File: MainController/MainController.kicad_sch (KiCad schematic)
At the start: 0 parts

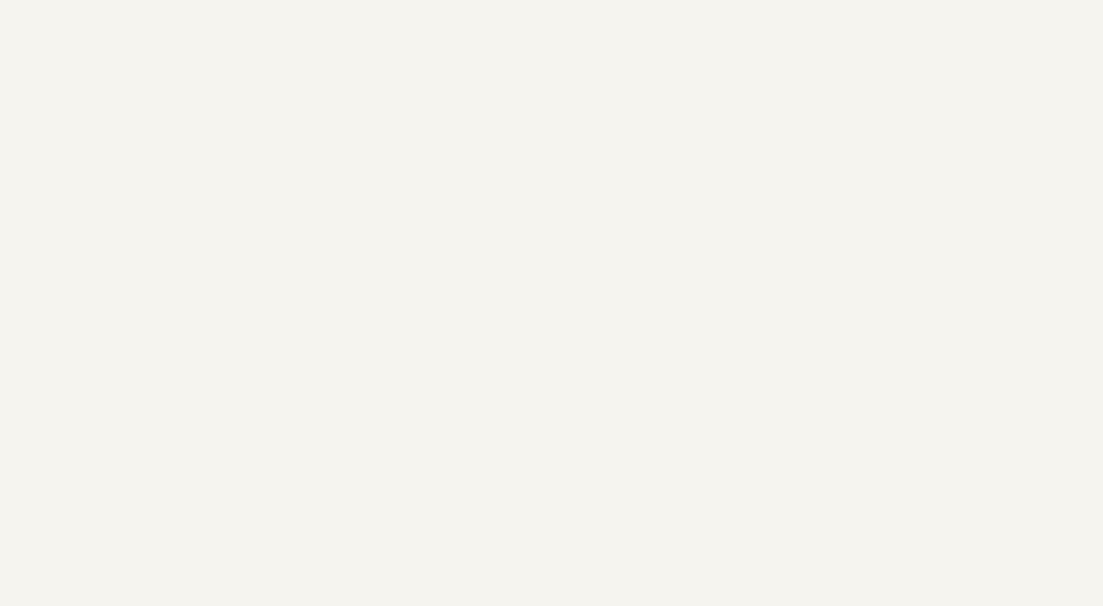
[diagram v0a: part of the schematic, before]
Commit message: WIP - Starting Voltage Measurement
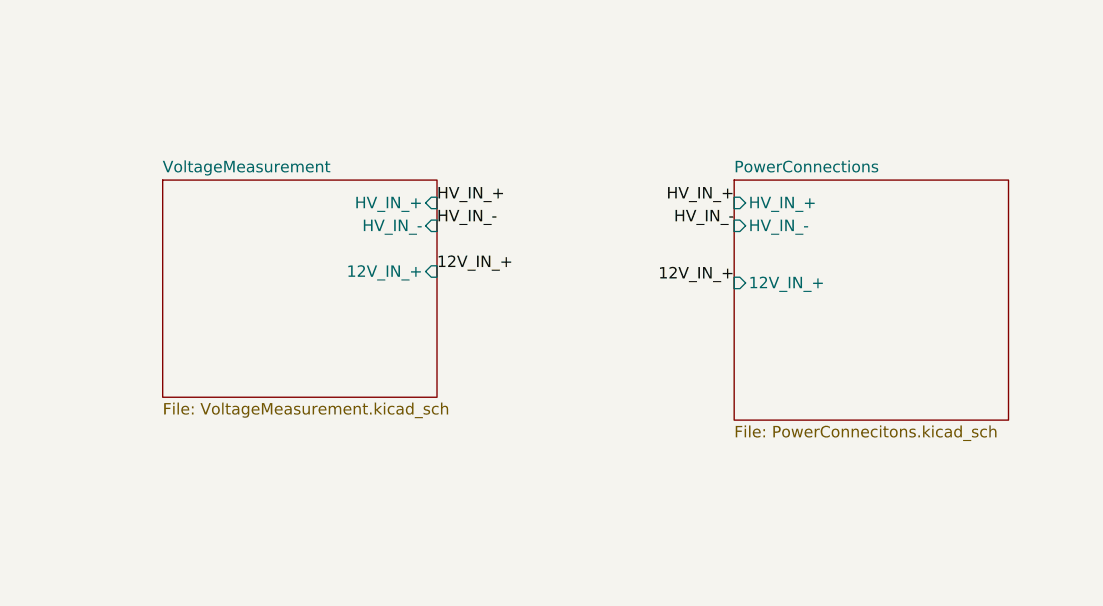
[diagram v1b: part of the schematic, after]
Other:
- added sheet PowerConnections (PowerConnecitons.kicad_sch)
- added sheet VoltageMeasurement (VoltageMeasurement.kicad_sch)
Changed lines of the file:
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@@
 	(generator_version "8.0")
 	(paper "A4")
+	(label "12V_IN_+"
+		(at 181.61 41.91 0)
+		(effects
+			(font
+				(size 1.27 1.27)
+			)
+			(justify left bottom)
+		)
+	)
+	(label "HV_IN_-"
+		(at 181.61 36.83 0)
+		(effects
+			(font
+				(size 1.27 1.27)
+			)
+			(justify left bottom)
+		)
+	)
+	(label "12V_IN_+"
+		(at 214.63 43.18 180)
+		(effects
+			(font
+				(size 1.27 1.27)
+			)
+			(justify right bottom)
+		)
+	)
+	(label "HV_IN_-"
+		(at 214.63 36.83 180)
+		(effects
+			(font
+				(size 1.27 1.27)
+			)
+			(justify right bottom)
+		)
+	)
+	(label "HV_IN_+"
+		(at 181.61 34.29 0)
+		(effects
+			(font
+				(size 1.27 1.27)
+			)
+			(justify left bottom)
+		)
+	)
+	(label "HV_IN_+"
+		(at 214.63 34.29 180)
+		(effects
+			(font
+				(size 1.27 1.27)
+			)
+			(justify right bottom)
+		)
+	)
 	(sheet
 		(at 17.78 82.55)
@@
 				)
 			)
+		)
+	)
+	(sheet
+		(at 151.13 31.75)
+		(size 30.48 24.13)
+		(fields_autoplaced yes)
+		(stroke
+			(width 0.1524)
+			(type solid)
+		)
+		(fill
+			(color 0 0 0 0.0000)
+		)
+		(property "Sheetname" "VoltageMeasurement"
+			(at 151.13 31.0384 0)
+			(effects
+				(font
+					(size 1.27 1.27)
+				)
+				(justify left bottom)
+			)
+		)
+		(property "Sheetfile" "VoltageMeasurement.kicad_sch"
+			(at 151.13 56.4646 0)
+			(effects
+				(font
+					(size 1.27 1.27)
+				)
+				(justify left top)
+			)
+		)
+		(pin "HV_IN_+" input
+			(at 181.61 34.29 0)
+			(effects
+				(font
+					(size 1.27 1.27)
+				)
+				(justify right)
+			)
+		)
+		(pin "HV_IN_-" input
+			(at 181.61 36.83 0)
+			(effects
+				(font
+					(size 1.27 1.27)
+				)
+				(justify right)
+			)
+		)
+		(pin "12V_IN_+" input
+			(at 181.61 41.91 0)
+			(effects
+				(font
+					(size 1.27 1.27)
+				)
+				(justify right)
+			)
+		)
+		(instances
+			(project "MainController"
+				(path "/e87d5277-7d46-4d0d-9217-730b2b1f3b51"
+					(page "7")
+				)
+			)
+		)
+	)
+	(sheet
+		(at 214.63 31.75)
+		(size 30.48 26.67)
+		(fields_autoplaced yes)
+		(stroke
+			(width 0.1524)
+			(type solid)
+		)
+		(fill
+			(color 0 0 0 0.0000)
+		)
+		(property "Sheetname" "PowerConnections"
+			(at 214.63 31.0384 0)
+			(effects
+				(font
+					(size 1.27 1.27)
+				)
+				(justify left bottom)
+			)
+		)
+		(property "Sheetfile" "PowerConnecitons.kicad_sch"
+			(at 214.63 59.0046 0)
+			(effects
+				(font
+					(size 1.27 1.27)
+				)
+				(justify left top)
+			)
+		)
+		(pin "HV_IN_+" input
+			(at 214.63 34.29 180)
+			(effects
+				(font
+					(size 1.27 1.27)
+				)
+				(justify left)
+			)
+		)
+		(pin "HV_IN_-" input
+			(at 214.63 36.83 180)
+			(effects
+				(font
+					(size 1.27 1.27)
+				)
+				(justify left)
+			)
+		)
+		(pin "12V_IN_+" input
+			(at 214.63 43.18 180)
+			(effects
+				(font
+					(size 1.27 1.27)
+				)
+				(justify left)
+			)
+		)
+		(instances
+			(project "MainController"
+				(path "/e87d5277-7d46-4d0d-9217-730b2b1f3b51"
+					(page "8")
+				)
+			)

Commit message: WIP - HV measurement may be done
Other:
- sheet MCU ports: added OUTN, OUTP; removed none
- sheet Power ports: added 3v3_iso; removed none
- sheet VoltageMeasurement ports: added OUTN, OUTP; removed none
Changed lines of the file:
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@@
 	(generator_version "8.0")
 	(paper "A4")
+	(label "OUTP"
+		(at 181.61 49.53 0)
+		(effects
+			(font
+				(size 1.27 1.27)
+			)
+			(justify left bottom)
+		)
+	)
+	(label "OUTN"
+		(at 179.07 91.44 90)
+		(effects
+			(font
+				(size 1.27 1.27)
+			)
+			(justify left bottom)
+		)
+	)
 	(label "12V_IN_+"
 		(at 181.61 41.91 0)
@@
 	(label "HV_IN_-"
 		(at 181.61 36.83 0)
+		(effects
+			(font
+				(size 1.27 1.27)
+			)
+			(justify left bottom)
+		)
+	)
+	(label "OUTP"
+		(at 181.61 91.44 90)
+		(effects
+			(font
+				(size 1.27 1.27)
+			)
+			(justify left bottom)
+		)
+	)
+	(label "OUTN"
+		(at 181.61 52.07 0)
 		(effects
 			(font
@@
 			)
 		)
+		(pin "3v3_iso" input
+			(at 81.28 138.43 90)
+			(effects
+				(font
+					(size 1.27 1.27)
+				)
+				(justify right)
+			)
+		)
 		(instances
 			(project "MainController"
@@
 			)
 		)
+		(pin "OUTN" input
+			(at 179.07 91.44 90)
+			(effects
+				(font
+					(size 1.27 1.27)
+				)
+				(justify right)
+			)
+		)
+		(pin "OUTP" input
+			(at 181.61 91.44 90)
+			(effects
+				(font
+					(size 1.27 1.27)
+				)
+				(justify right)
+			)
+		)
 		(instances
 			(project "MainController"
@@
 			(effects
 				(font
+					(size 1.27 1.27)
+				)
+				(justify right)
+			)
+		)
+		(pin "OUTN" input
+			(at 181.61 52.07 0)
+			(effects
+				(font
+					(size 1.27 1.27)
+				)
+				(justify right)
+			)
+		)
+		(pin "OUTP" input
+			(at 181.61 49.53 0)
+			(effects
+				(font

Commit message: WIP likely need to switch 12V signalling around
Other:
- sheet Switches ports: added 12V_IN_+; removed none
- sheet VoltageMeasurement ports: added 3v3_iso; removed none
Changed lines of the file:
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@@
+		)
+	)
+	(label "3v3_iso"
+		(at 81.28 138.43 90)
+		(effects
+			(font
+				(size 1.27 1.27)
+			)
+			(justify left bottom)
 		)
 	)
@@
 		)
 	)
+	(label "12V_IN_+"
+		(at 45.72 83.82 0)
+		(effects
+			(font
+				(size 1.27 1.27)
+			)
+			(justify left bottom)
+		)
+	)
 	(label "OUTN"
 		(at 181.61 52.07 0)
@@
 		)
 	)
+	(label "CAN_L"
+		(at 45.72 59.69 0)
+		(effects
+			(font
+				(size 1.27 1.27)
+			)
+			(justify left bottom)
+		)
+	)
+	(label "3v3_iso"
+		(at 151.13 48.26 180)
+		(effects
+			(font
+				(size 1.27 1.27)
+			)
+			(justify right bottom)
+		)
+	)
+	(label "CAN_H"
+		(at 45.72 57.15 0)
+		(effects
+			(font
+				(size 1.27 1.27)
+			)
+			(justify left bottom)
+		)
+	)
 	(label "12V_IN_+"
 		(at 214.63 43.18 180)
@@
 				)
 				(justify left top)
+			)
+		)
+		(pin "12V_IN_+" input
+			(at 45.72 83.82 0)
+			(effects
+				(font
+					(size 1.27 1.27)
+				)
+				(justify right)
 			)
 		)
@@
 			)
 		)
+		(pin "3v3_iso" input
+			(at 151.13 48.26 180)
+			(effects
+				(font
+					(size 1.27 1.27)
+				)
+				(justify left)
+			)
+		)

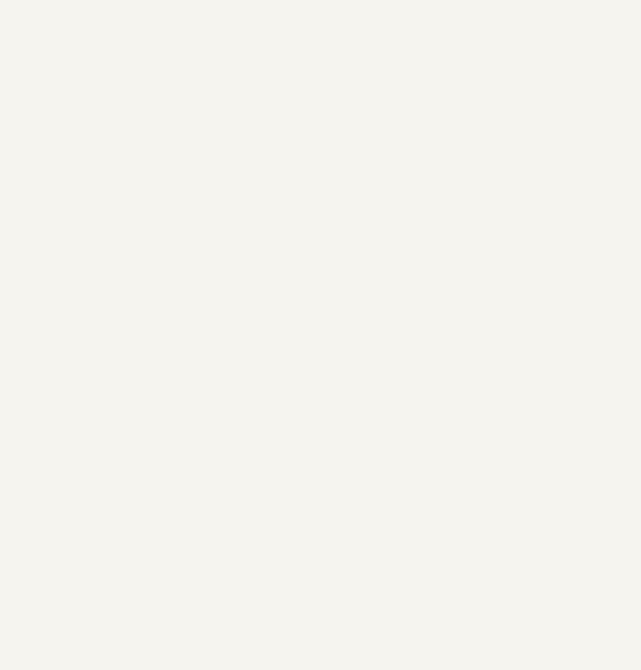
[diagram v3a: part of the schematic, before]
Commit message: Adding Motor Controller Page
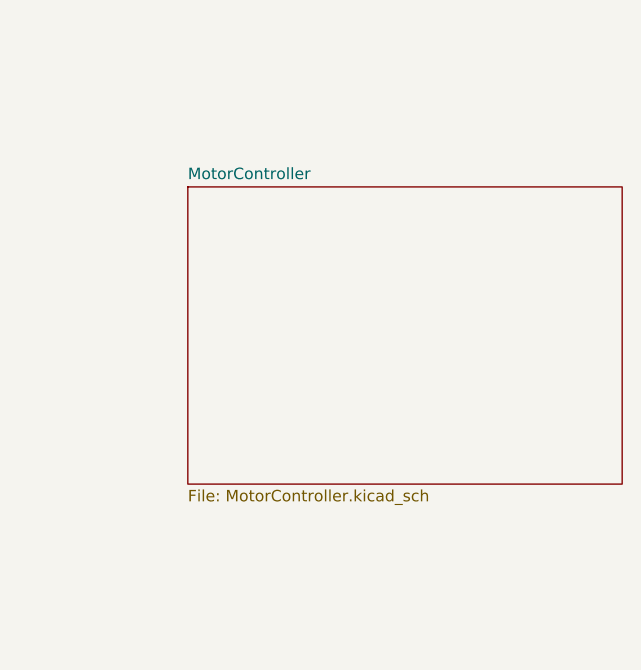
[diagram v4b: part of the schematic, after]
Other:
- added sheet MotorController (MotorController.kicad_sch)
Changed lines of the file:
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@@
+	)
+	(sheet
+		(at 224.79 111.76)
+		(size 48.26 33.02)
+		(fields_autoplaced yes)
+		(stroke
+			(width 0.1524)
+			(type solid)
+		)
+		(fill
+			(color 0 0 0 0.0000)
+		)
+		(property "Sheetname" "MotorController"
+			(at 224.79 111.0484 0)
+			(effects
+				(font
+					(size 1.27 1.27)
+				)
+				(justify left bottom)
+			)
+		)
+		(property "Sheetfile" "MotorController.kicad_sch"
+			(at 224.79 145.3646 0)
+			(effects
+				(font
+					(size 1.27 1.27)
+				)
+				(justify left top)
+			)
+		)
+		(instances
+			(project "MainController"
+				(path "/e87d5277-7d46-4d0d-9217-730b2b1f3b51"
+					(page "9")
+				)
+			)
+		)
 	)
 	(sheet
